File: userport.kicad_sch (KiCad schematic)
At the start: 41 parts, among them J3 C64_User_Port, J4 Mini-DIN-8-With-Shield, J5 C64_Tape_Port, J6 OKR-T/3-W12-C, U1 74LS595, U10 74LS125, U11 74LS595, U2 74LVC165, U3 74LS125, U4 74LS595, U5 74LVC165, U6 74LS595, U7 74LVC165, U8 74LS125, U9 74LS125

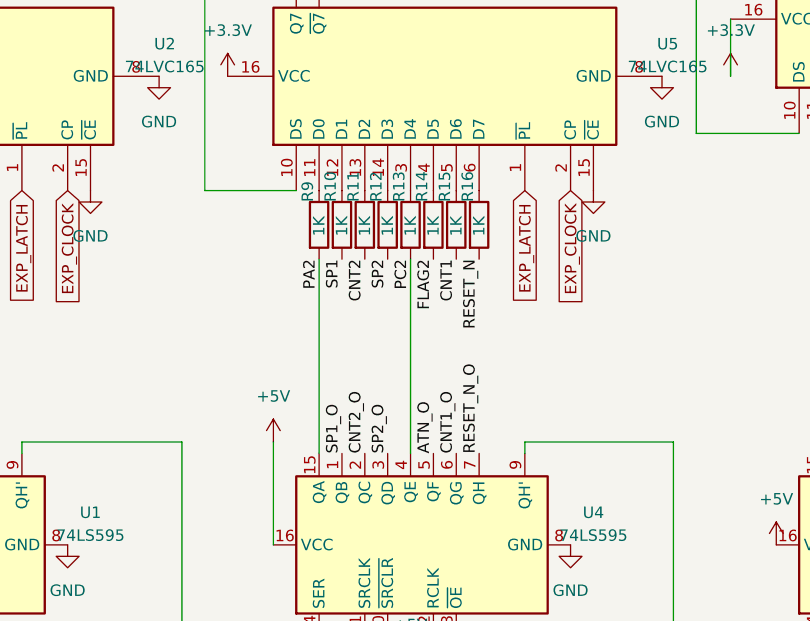
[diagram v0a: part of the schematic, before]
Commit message: /PC2 is output only
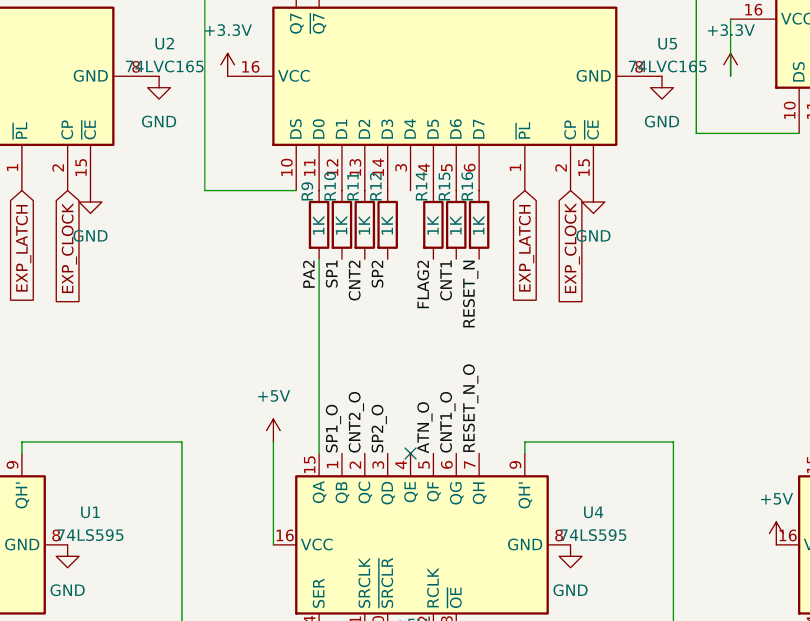
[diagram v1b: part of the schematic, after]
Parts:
- removed R13: 1K, snapeda:Labeled Resistor, symbol Device:R
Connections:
- net PC2: no longer U4.4 (QE)
- no-connect marks 13 -> 14
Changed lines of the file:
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@@
   (no_connect (at 147.32 39.37))
   (no_connect (at 144.78 39.37))
+  (no_connect (at 99.06 74.93))
   (no_connect (at 152.4 74.93))
   (no_connect (at 49.53 182.88))
@@
     (stroke (width 0) (type default) (color 0 0 0 0))
   )
-  (wire (pts (xy 99.06 53.34) (xy 99.06 74.93))
-    (stroke (width 0) (type default) (color 0 0 0 0))
-  )
   (wire (pts (xy 62.23 162.56) (xy 69.85 162.56))
     (stroke (width 0) (type default) (color 0 0 0 0))
@@
     (effects (font (size 1.27 1.27)) (justify left bottom))
   )
-  (label "PC2" (at 99.06 53.34 270)
-    (effects (font (size 1.27 1.27)) (justify right bottom))
-  )
   (label "DATA_3" (at 40.64 60.96 90)
     (effects (font (size 1.27 1.27)) (justify left bottom))
@@
     (pin "1")
   )
-  (symbol (lib_id "Device:R") (at 99.06 49.53 0) (unit 1)
-    (in_bom yes) (on_board yes)
-    (property "Reference" "R13" (id 0) (at 97.79 46.99 90)
-      (effects (font (size 1.27 1.27)) (justify left))
-    )
-    (property "Value" "1K" (id 1) (at 99.06 50.8 90)
-      (effects (font (size 1.27 1.27)) (justify left))
-    )
-    (property "Footprint" "snapeda:Labeled Resistor" (id 2) (at 97.282 49.53 90)
-      (effects (font (size 1.27 1.27)) hide)
-    )
-    (property "Datasheet" "~" (id 3) (at 99.06 49.53 0)
-      (effects (font (size 1.27 1.27)) hide)
-    )
-    (pin "1")
-    (pin "2")
-  )
   (symbol (lib_id "Device:R") (at 88.9 49.53 0) (unit 1)

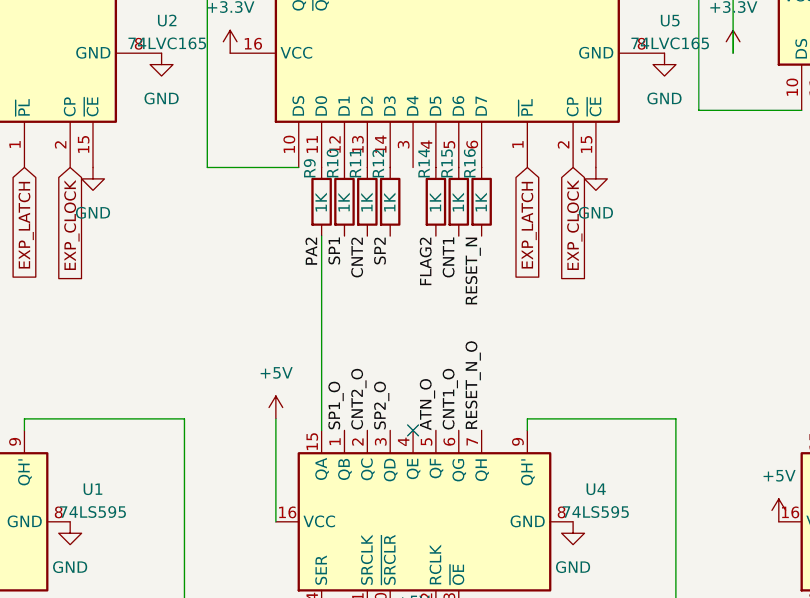
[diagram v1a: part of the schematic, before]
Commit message: remote more redundant nets
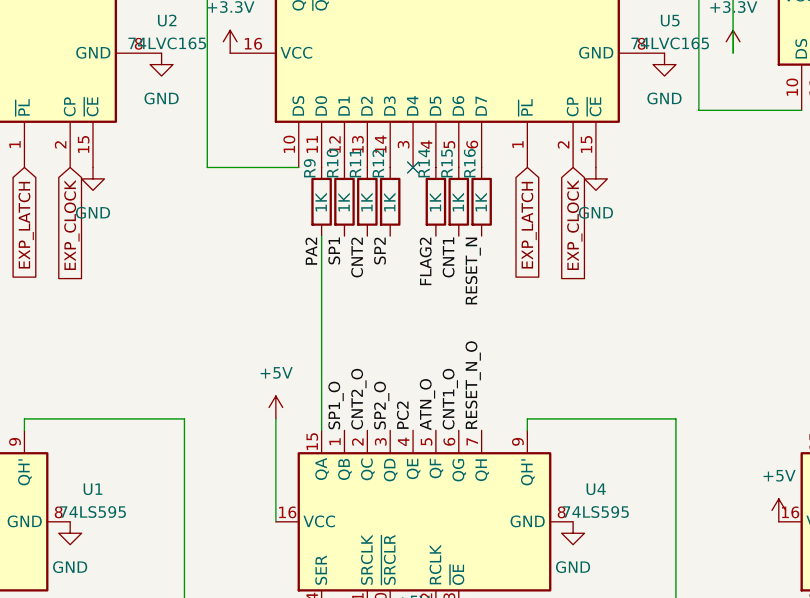
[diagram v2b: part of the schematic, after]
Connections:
- net PC2: now also U4.4 (QE)
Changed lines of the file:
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@@
   (no_connect (at 147.32 39.37))
   (no_connect (at 144.78 39.37))
-  (no_connect (at 99.06 74.93))
+  (no_connect (at 99.06 45.72))
   (no_connect (at 152.4 74.93))
   (no_connect (at 49.53 182.88))
@@
     (effects (font (size 1.27 1.27)) (justify left bottom))
   )
+  (label "PC2" (at 99.06 74.93 90)
+    (effects (font (size 1.27 1.27)) (justify left bottom))
+  )

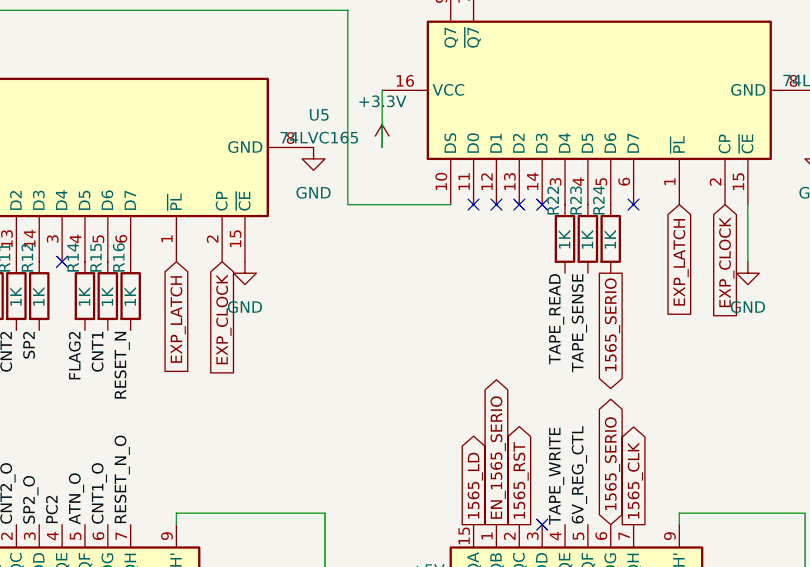
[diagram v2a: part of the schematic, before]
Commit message: move JTAG headers to better align with PCB and tape port hole
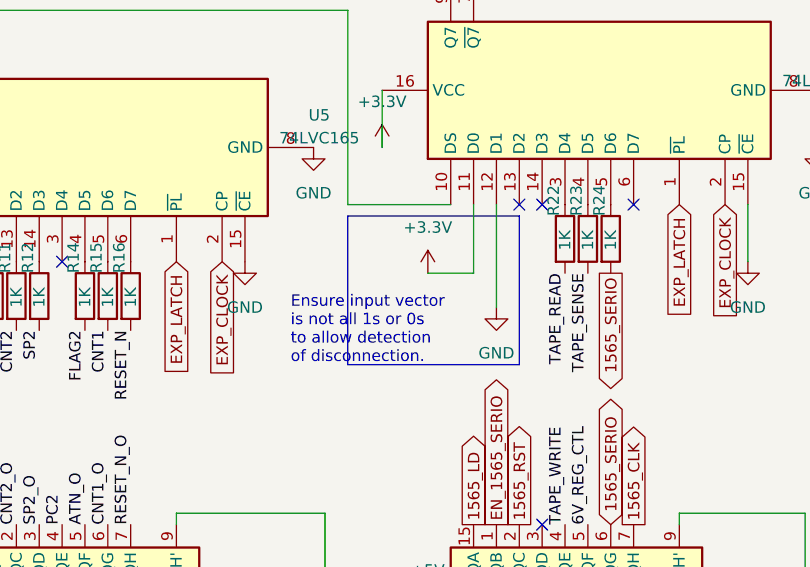
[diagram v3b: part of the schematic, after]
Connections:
- net +3V3: now also U7.11 (D0)
- net GND: now also U7.12 (D1)
- no-connect marks 14 -> 12
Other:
- note added: "Ensure input vector is not all 1s or 0s to allow detection of disconnection."
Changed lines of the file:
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@@
   (no_connect (at 149.86 39.37))
   (no_connect (at 152.4 39.37))
-  (no_connect (at 147.32 39.37))
-  (no_connect (at 144.78 39.37))
   (no_connect (at 99.06 45.72))
   (no_connect (at 152.4 74.93))
@@
     (stroke (width 0) (type default) (color 0 0 0 0))
   )
+  (polyline (pts (xy 149.86 57.15) (xy 130.81 57.15))
+    (stroke (width 0) (type default) (color 0 0 0 0))
+  )
   (wire (pts (xy 138.43 156.21) (xy 149.86 156.21))
     (stroke (width 0) (type default) (color 0 0 0 0))
@@
     (stroke (width 0) (type default) (color 0 0 0 0))
   )
+  (wire (pts (xy 147.32 39.37) (xy 147.32 50.8))
+    (stroke (width 0) (type default) (color 0 0 0 0))
+  )
   (wire (pts (xy 76.2 45.72) (xy 86.36 45.72))
     (stroke (width 0) (type default) (color 0 0 0 0))
@@
     (stroke (width 0) (type default) (color 0 0 0 0))
   )
+  (wire (pts (xy 139.7 46.99) (xy 144.78 46.99))
+    (stroke (width 0) (type default) (color 0 0 0 0))
+  )
   (wire (pts (xy 128.27 73.66) (xy 128.27 95.25))
     (stroke (width 0) (type default) (color 0 0 0 0))
@@
     (stroke (width 0) (type default) (color 0 0 0 0))
   )
+  (wire (pts (xy 144.78 39.37) (xy 144.78 46.99))
+    (stroke (width 0) (type default) (color 0 0 0 0))
+  )
   (wire (pts (xy 62.23 162.56) (xy 69.85 162.56))
     (stroke (width 0) (type default) (color 0 0 0 0))
@@
     (stroke (width 0) (type default) (color 0 0 0 0))
   )
+  (polyline (pts (xy 130.81 40.64) (xy 149.86 40.64))
+    (stroke (width 0) (type default) (color 0 0 0 0))
+  )
+  (polyline (pts (xy 130.81 40.64) (xy 130.81 57.15))
+    (stroke (width 0) (type default) (color 0 0 0 0))
+  )
   (wire (pts (xy 154.94 99.06) (xy 152.4 99.06))
     (stroke (width 0) (type default) (color 0 0 0 0))
@@
   )
   (wire (pts (xy 62.23 177.8) (xy 69.85 177.8))
+    (stroke (width 0) (type default) (color 0 0 0 0))
+  )
+  (polyline (pts (xy 149.86 40.64) (xy 149.86 57.15))
     (stroke (width 0) (type default) (color 0 0 0 0))
   )
@@
     (effects (font (size 1.27 1.27)) (justify left bottom))
   )
+  (text "Ensure input vector\nis not all 1s or 0s\nto allow detection\nof disconnection."
+    (at 124.46 57.15 0)
+    (effects (font (size 1.27 1.27)) (justify left bottom))
+  )
   (text "C65-compatible 1565 External Dumb\nFloppy Interface"
     (at 54.61 121.92 0)
@@
     (pin "1")
     (pin "2")
+  )
+  (symbol (lib_id "power:+3.3V") (at 139.7 46.99 0) (unit 1)
+    (in_bom yes) (on_board yes) (fields_autoplaced)
+    (property "Reference" "#PWR0101" (id 0) (at 139.7 50.8 0)
+      (effects (font (size 1.27 1.27)) hide)
+    )
+    (property "Value" "+3.3V" (id 1) (at 139.7 41.91 0))
+    (property "Footprint" "" (id 2) (at 139.7 46.99 0)
+      (effects (font (size 1.27 1.27)) hide)
+    )
+    (property "Datasheet" "" (id 3) (at 139.7 46.99 0)
+      (effects (font (size 1.27 1.27)) hide)
+    )
+    (pin "1")
   )
   (symbol (lib_id "power:GND") (at 130.81 140.97 0) (unit 1)
@@
     (pin "13")
   )
+  (symbol (lib_id "power:GND") (at 147.32 50.8 0) (unit 1)
+    (in_bom yes) (on_board yes) (fields_autoplaced)
+    (property "Reference" "#PWR0102" (id 0) (at 147.32 57.15 0)
+      (effects (font (size 1.27 1.27)) hide)
+    )
+    (property "Value" "GND" (id 1) (at 147.32 55.88 0))
+    (property "Footprint" "" (id 2) (at 147.32 50.8 0)
+      (effects (font (size 1.27 1.27)) hide)
+    )
+    (property "Datasheet" "" (id 3) (at 147.32 50.8 0)
+      (effects (font (size 1.27 1.27)) hide)
+    )
+    (pin "1")
+  )
   (symbol (lib_id "74xx:74LS595") (at 99.06 85.09 90) (unit 1)

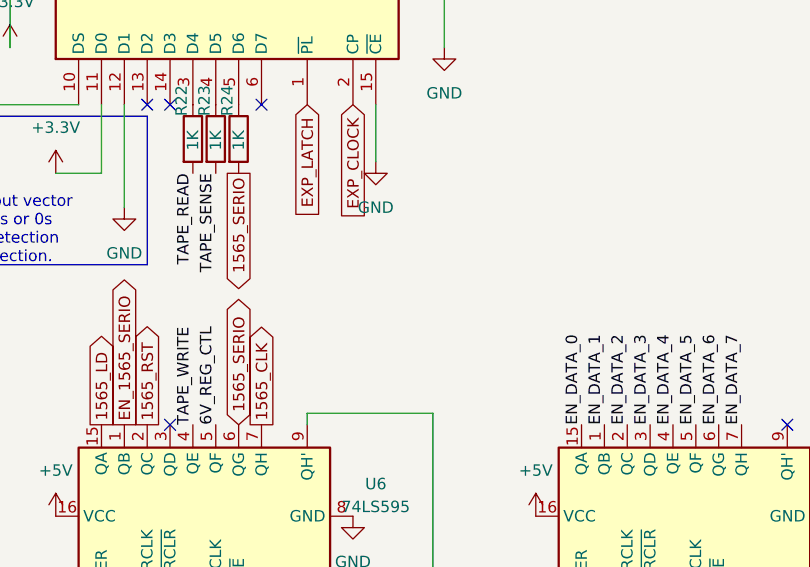
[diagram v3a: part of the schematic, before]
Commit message: add 3.3V zener to tape sense input
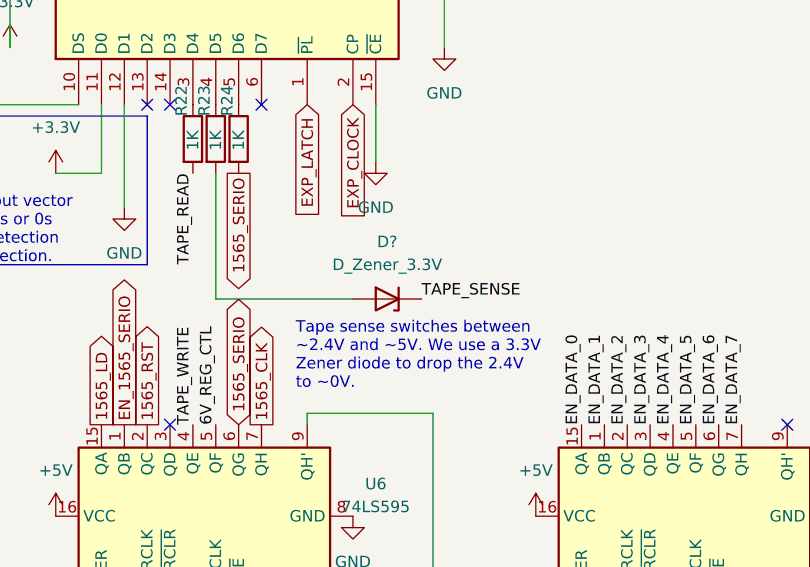
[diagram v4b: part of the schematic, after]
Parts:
- added D?: D_Zener_3.3V, Diode_THT:D_A-405_P10.16mm_Horizontal, symbol Device:D_Zener
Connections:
- net TAPE_SENSE: now also D?.1 (K); no longer R23.2
- new net: D?.2 (A), R23.2
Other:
- note added: "Tape sense switches between ~2.4V and ~5V. We use a 3.3V Zener diode to drop the 2.4V to ~0V."

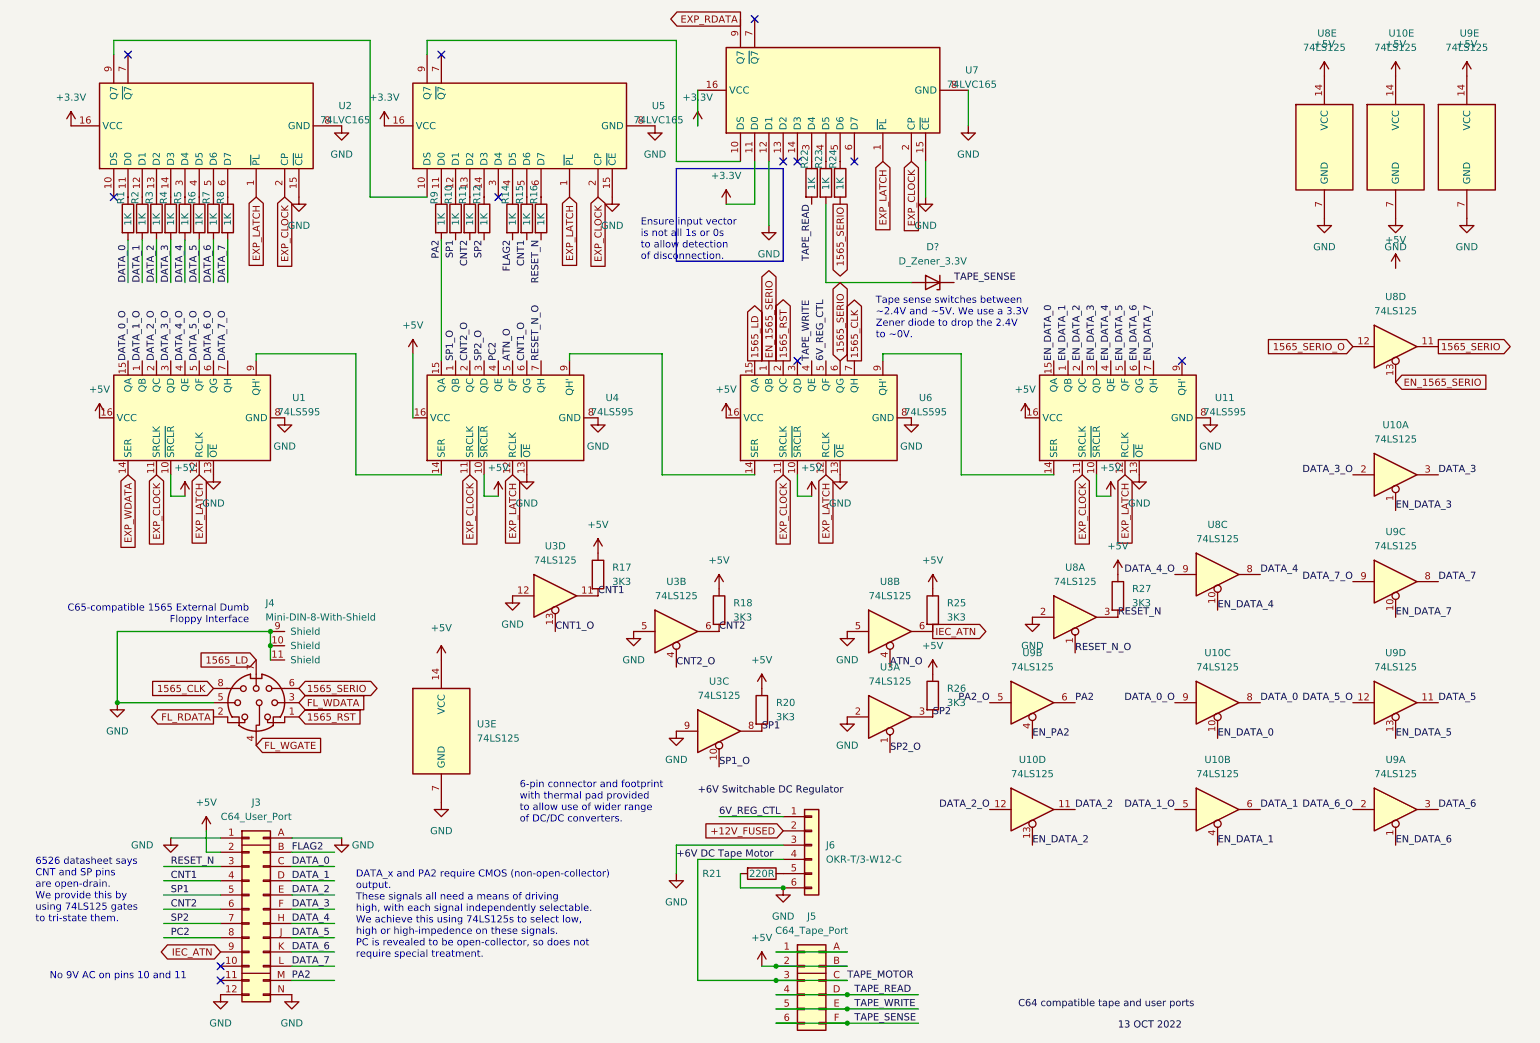
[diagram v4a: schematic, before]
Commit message: connect tape GND pin to GND
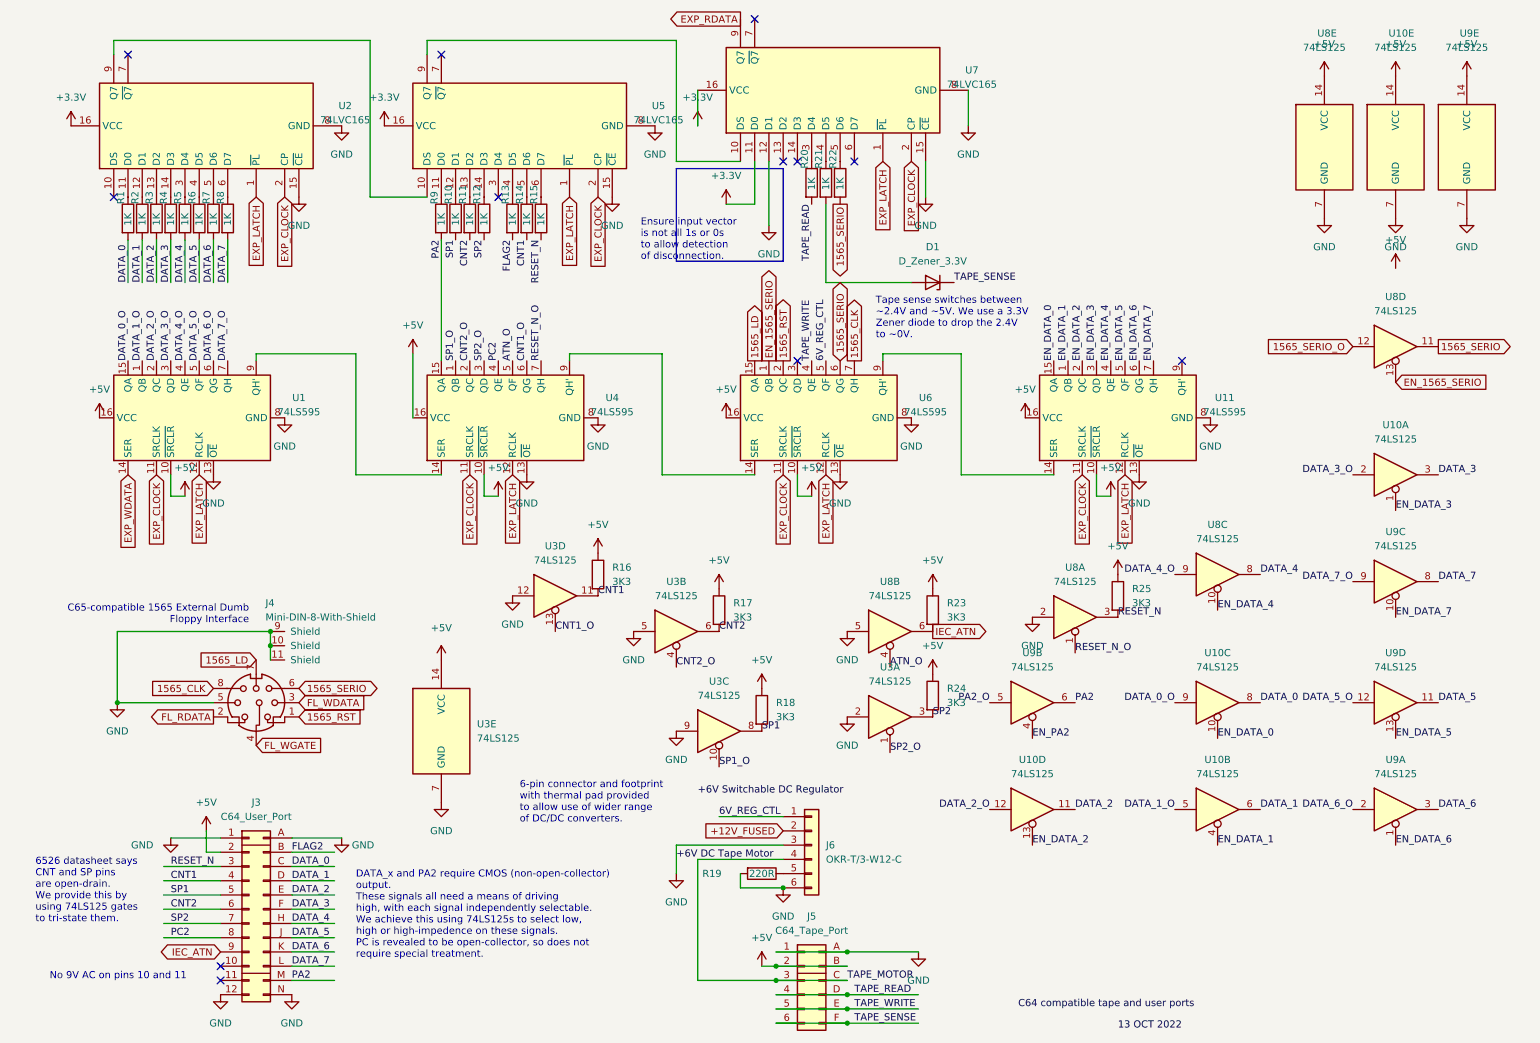
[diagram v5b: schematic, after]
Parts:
- gave numbers to parts that had none: 1
- renumbered R14 to R13, R15 to R14, R16 to R15, R17 to R16, R18 to R17, R20 to R18, R21 to R19, R22 to R20, R23 to R21, R24 to R22, R25 to R23, R26 to R24, R27 to R25
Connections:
- net GND: now also J5.1 (Pin_1), J5.A (Pin_A)
